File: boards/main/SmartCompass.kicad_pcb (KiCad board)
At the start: 4 copper layers, 70 x 70 mm, 78 parts, among them IC1 Wio-SX1262, J1 SWD HEADER, J3 FH12-10S-0.5SH(55), J4 FH12-10S-0.5SH(55), J5 IPEX, P1 BUTTON_PADS, Q1 DMP2045U, U1 BMD-340-A-R, U2 S25FL064LABNFI043, U3 RT9080-33GJ5, U4 MCP73831T-2ACI_OT, U5 MAX17048G_T10, U6 BNO086, U7 DRV2605LDGSR, U8 MAX-M10S-00B, X1 USB4085-GF-A, Y1 32.768KHZ, Y2 32.768KHZ

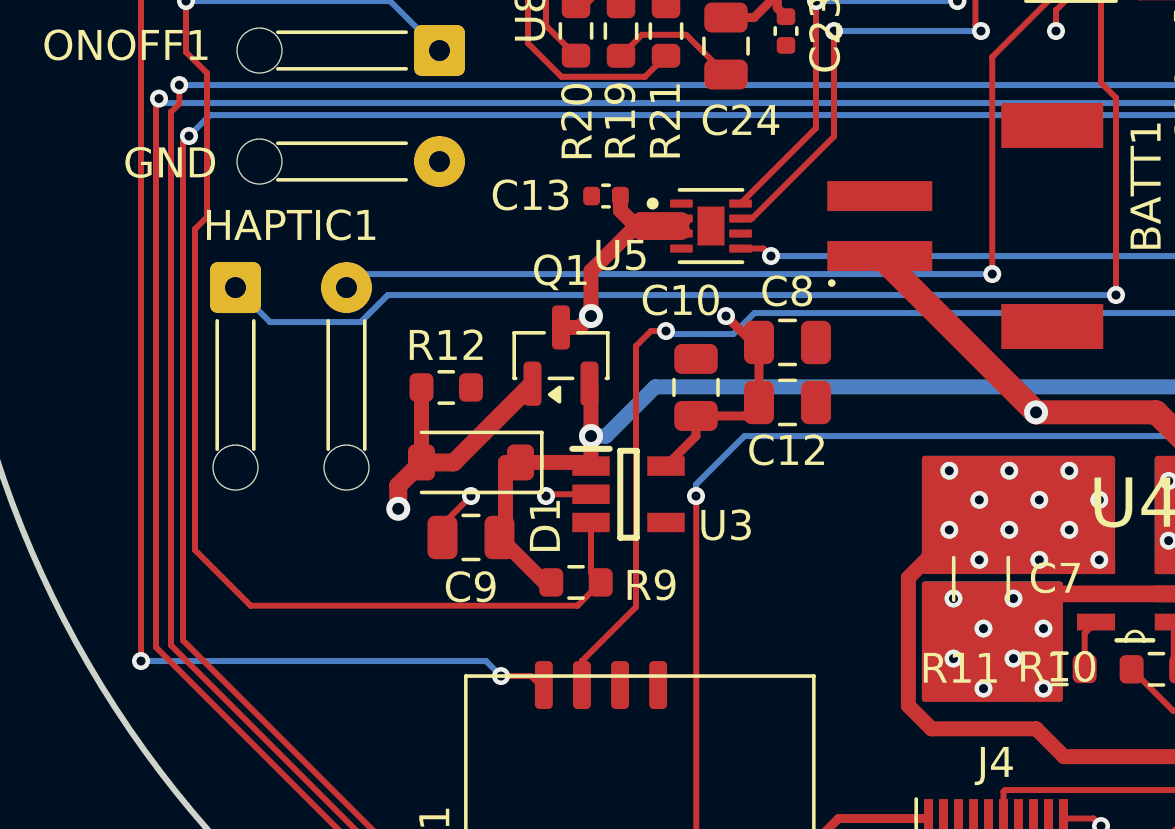
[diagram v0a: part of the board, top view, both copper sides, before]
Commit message: update the board layout to add extra copper on the schottky diode
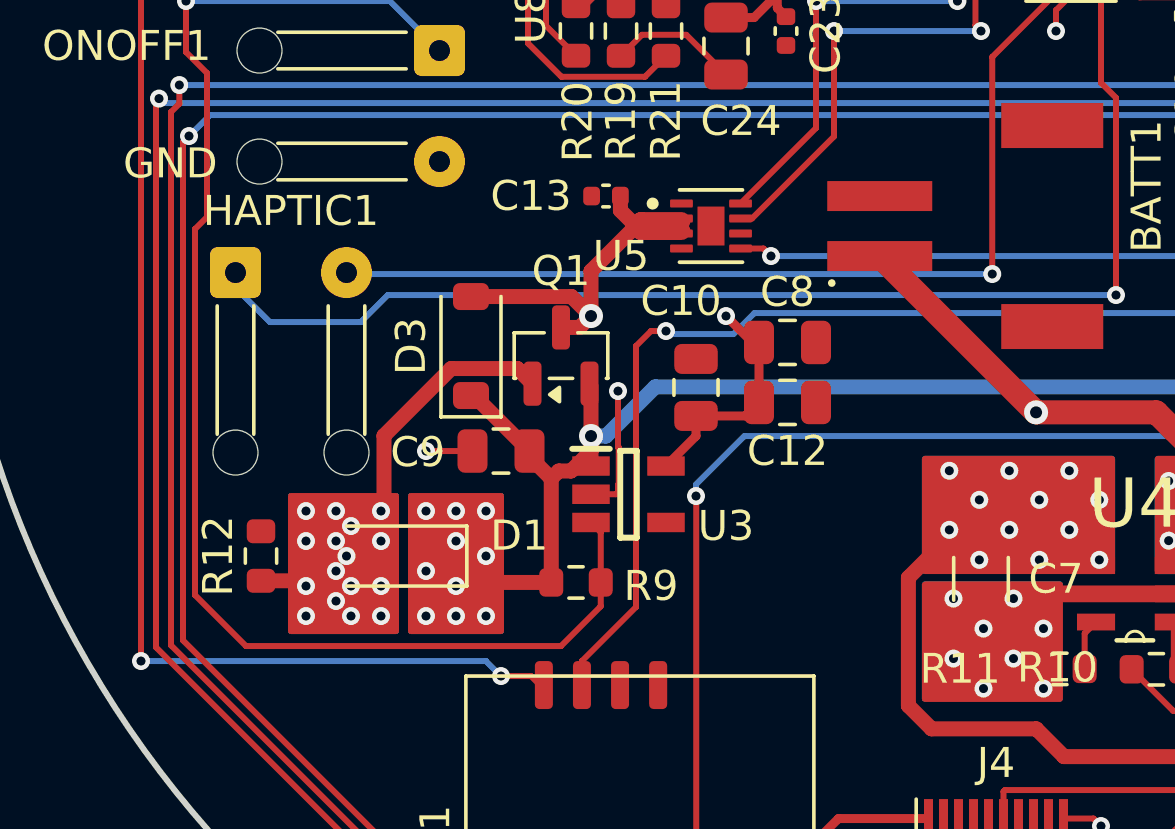
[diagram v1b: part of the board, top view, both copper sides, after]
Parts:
- added D3: SS1040-AU, Diode_SMD:D_SOD-123, F.Cu at (82.5, 107.0)
- D1: value MBR0540 -> SS1040-AU
- R12: value 100K -> 4.7K
- R9: value 100K -> 1M
- moved R12 8.35 mm to (75.5, 114.0), turned to 90 degrees
- moved D1 4.00 mm to (80.0, 114.0)
- moved C9 3.05 mm to (83.5, 110.5)
- moved HAPTIC1 0.50 mm to (74.7, 104.5)
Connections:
- R12 pad 1: GND -> VBUS
- R12 pad 2: VBUS -> GND
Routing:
- net VSYS: track 80.0 -> 85.4 mm, vias 3 -> 13
- net +BATT: track 42.1 -> 46.4 mm
- net GND: track 92.4 -> 95.5 mm
- net Net-(ONOFF1-Pin_1): track 44.6 -> 47.1 mm
- net VBUS: track 143.1 -> 144.7 mm, vias 15 -> 30

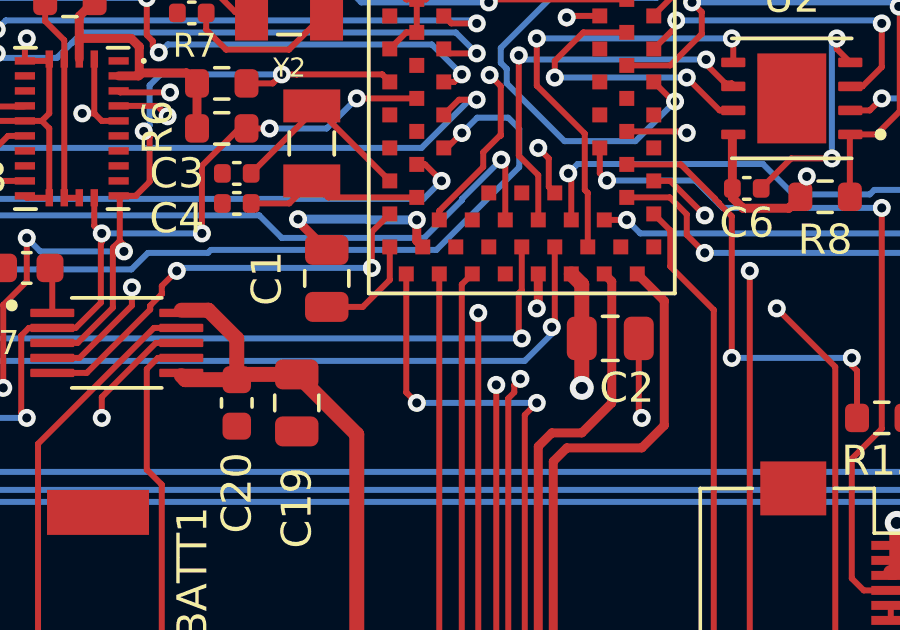
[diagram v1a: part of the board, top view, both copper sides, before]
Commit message: Reduce the capacitance on the VBUS line to below 10uF by removing the cap by the MCU. It wasnt needed anyway
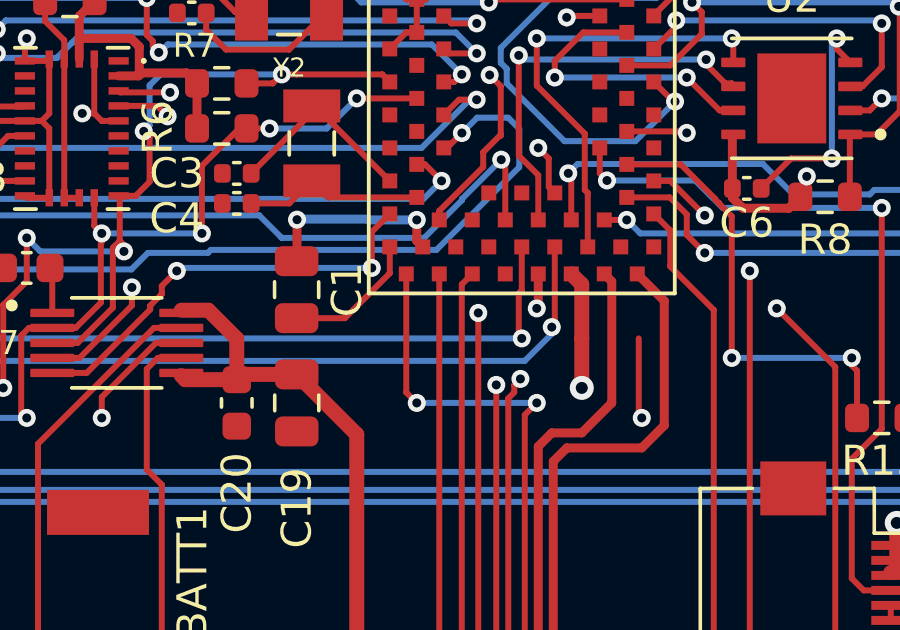
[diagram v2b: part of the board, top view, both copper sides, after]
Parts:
- removed C2: 10uF, Capacitor_SMD:C_0805_2012Metric
- moved C1 1.07 mm to (108.5, 92.2)
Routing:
- net GND: track 95.5 -> 96.5 mm
